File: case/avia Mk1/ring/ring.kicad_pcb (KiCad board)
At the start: 2 copper layers, 44 x 43.6 mm, 1 part

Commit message: corrected ring
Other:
- board text added: "avia ring v1.1"
- board text removed: "avia ring v1.0"
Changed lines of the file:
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@@
   (gr_line (start 162.476247 110.034954) (end 162.233575 109.716945) (layer "F.SilkS") (width 0.12))
   (gr_line (start 167.756337 103.786811) (end 167.401359 103.602393) (layer "F.SilkS") (width 0.12))
-  (gr_line (start 152.67 78.22) (end 153.48 78.32) (layer "F.SilkS") (width 0.1))
   (gr_line (start 157.675734 77.525941) (end 157.537261 77.901234) (layer "F.SilkS") (width 0.12))
   (gr_line (start 150.354831 113.833576) (end 150.370555 113.433861) (layer "F.SilkS") (width 0.12))
   (gr_line (start 145.720647 77.150237) (end 145.83725 77.53289) (layer "F.SilkS") (width 0.12))
   (gr_line (start 166.93 101.14) (end 167.02 101.18) (layer "F.SilkS") (width 0.12))
-  (gr_line (start 152.594209 79.031849) (end 152.67 78.22) (layer "F.SilkS") (width 0.1))
   (gr_line (start 132.492692 93.140089) (end 133.387785 93.234167) (layer "F.SilkS") (width 0.12))
   (gr_line (start 168.268998 102.726321) (end 167.446786 102.360249) (layer "F.SilkS") (width 0.12))
@@
     (effects (font (size 0.5 1.5) (thickness 0.125)))
   )
-  (gr_text "avia ring v1.0" (at 156.29 111.37) (layer "B.SilkS")
+  (gr_text "avia ring v1.1" (at 156.29 111.37) (layer "B.SilkS")
     (effects (font (size 0.6 1) (thickness 0.15)) (justify left mirror))
   )
@@
     (effects (font (size 0.7 1) (thickness 0.12)))
   )
-  (gr_text "KM" (at 154.06 78.17 -10.09) (layer "F.SilkS")
-    (effects (font (size 0.5 0.5) (thickness 0.08)))
-  )
   (gr_text "|" (at 135.542933 98.078105 100.81) (layer "F.SilkS")

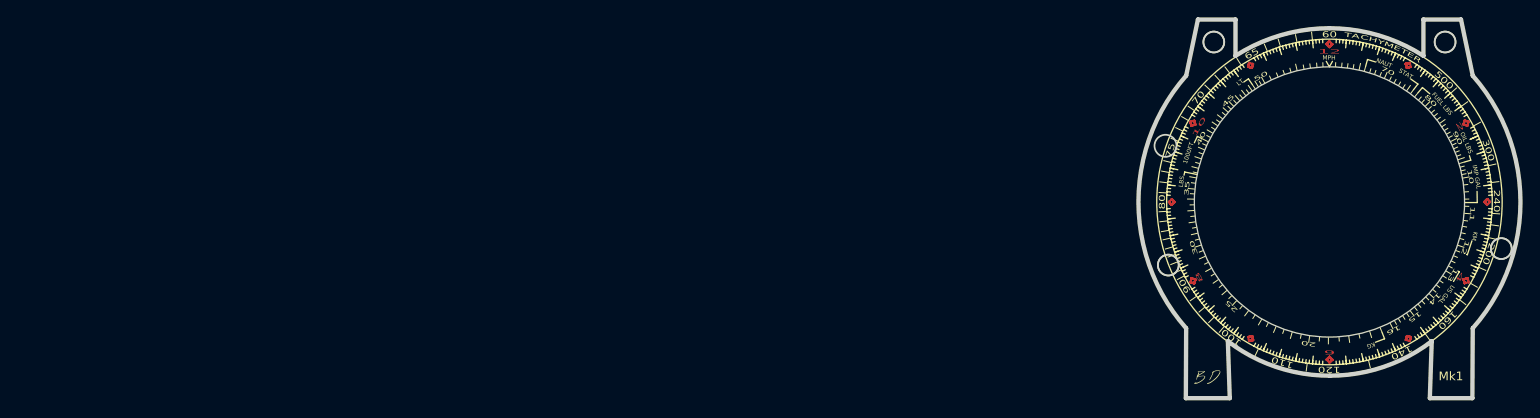
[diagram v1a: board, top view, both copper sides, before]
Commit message: added SR manual
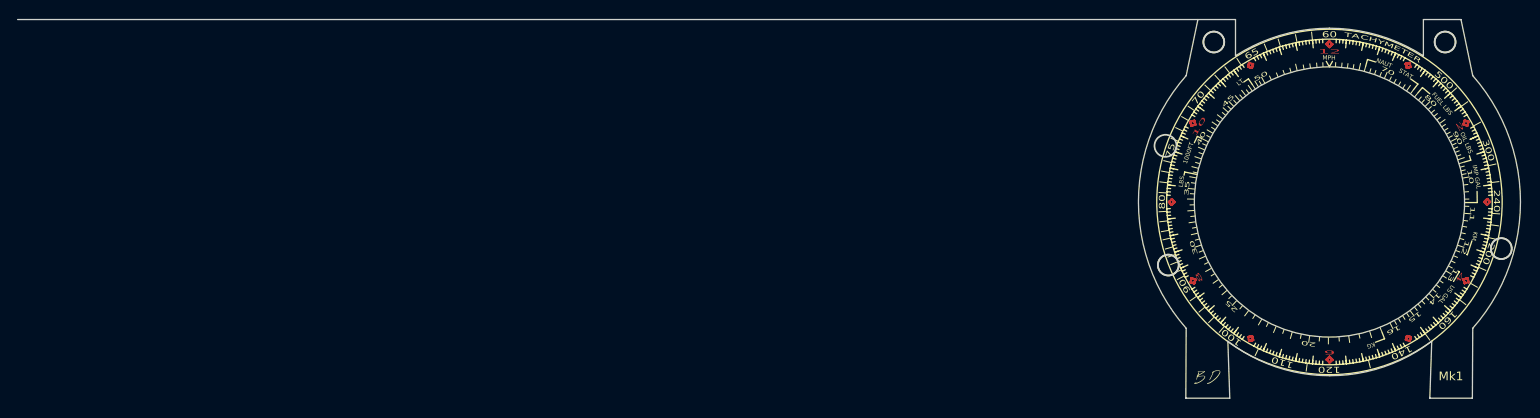
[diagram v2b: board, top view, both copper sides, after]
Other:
- board size 44 x 43.6 mm -> 173.1 x 43.6 mm
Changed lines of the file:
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@@
   (gr_line (start 137.64 108.6) (end 137.64 81.6) (layer "Cmts.User") (width 0.15))
   (gr_circle (center 164.46 76.68) (end 166.759609 76.68) (layer "Cmts.User") (width 0.15) (fill none))
+  (gr_circle (center 170.94 100.47) (end 173.239609 100.47) (layer "Cmts.User") (width 0.15) (fill none))
   (gr_line (start 167.04 79.2) (end 135.24 111) (layer "Cmts.User") (width 0.15))
   (gr_line (start 167.04 79.2) (end 167.04 116.52) (layer "Cmts.User") (width 0.15))
@@
   (gr_line (start 137.64 81.6) (end 137.64 79.2) (layer "Cmts.User") (width 0.15))
   (gr_line (start 137.64 81.6) (end 164.64 81.6) (layer "Cmts.User") (width 0.15))
-  (gr_arc (start 167.643267 80.553709) (mid 173.138918 95.100001) (end 167.643266 109.646293) (layer "Edge.Cuts") (width 0.5))
-  (gr_arc (start 151.18 115.11) (mid 144.981345 114.096892) (end 139.44 111.14) (layer "Edge.Cuts") (width 0.5))
-  (gr_line (start 162.92 111.14) (end 162.7 117.7) (layer "Edge.Cuts") (width 0.5))
-  (gr_arc (start 151.14 75.09) (mid 156.77909 75.901022) (end 161.961066 78.268344) (layer "Edge.Cuts") (width 0.5))
-  (gr_circle (center 151.14 95.1) (end 166.7 95.1) (layer "Edge.Cuts") (width 0.1) (fill none))
-  (gr_line (start 166.29 74.09) (end 167.643267 80.553709) (layer "Edge.Cuts") (width 0.5))
+  (gr_arc (start 167.643267 80.553709) (mid 173.139852 95.100001) (end 167.643266 109.646293) (layer "Edge.Cuts") (width 0.05))
+  (gr_arc (start 151.18 115.11) (mid 144.981385 114.096772) (end 139.44 111.14) (layer "Edge.Cuts") (width 0.05))
+  (gr_line (start 162.92 111.14) (end 162.7 117.7) (layer "Edge.Cuts") (width 0.05))
+  (gr_arc (start 151.14 75.09) (mid 156.778828 75.901912) (end 161.961066 78.268344) (layer "Edge.Cuts") (width 0.05))
+  (gr_circle (center 151.14 95.1) (end 166.7 95.1) (layer "Edge.Cuts") (width 0.05) (fill none))
+  (gr_line (start 166.29 74.09) (end 167.643267 80.553709) (layer "Edge.Cuts") (width 0.05))
   (gr_circle (center 132.58 102.37) (end 133.78 102.37) (layer "Edge.Cuts") (width 0.2) (fill none))
-  (gr_line (start 167.643266 109.646293) (end 167.6 117.7) (layer "Edge.Cuts") (width 0.5))
-  (gr_line (start 140.32 74.09) (end 140.32 78.27) (layer "Edge.Cuts") (width 0.5))
-  (gr_line (start 140.32 74.09) (end 135.99 74.09) (layer "Edge.Cuts") (width 0.5))
+  (gr_line (start 167.643266 109.646293) (end 167.6 117.7) (layer "Edge.Cuts") (width 0.05))
+  (gr_line (start 140.32 74.09) (end 140.32 78.27) (layer "Edge.Cuts") (width 0.05))
+  (gr_line (start 140.32 74.09) (end 0.05 74.09) (layer "Edge.Cuts") (width 0.05))
   (gr_circle (center 170.93 100.47) (end 172.13 100.47) (layer "Edge.Cuts") (width 0.2) (fill none))
-  (gr_line (start 161.96 74.09) (end 161.96 78.27) (layer "Edge.Cuts") (width 0.5))
-  (gr_line (start 139.66 117.7) (end 134.6 117.7) (layer "Edge.Cuts") (width 0.5))
-  (gr_arc (start 162.92 111.14) (mid 157.378655 114.096893) (end 151.18 115.11) (layer "Edge.Cuts") (width 0.5))
-  (gr_line (start 139.66 117.7) (end 139.44 111.14) (layer "Edge.Cuts") (width 0.5))
-  (gr_line (start 162.7 117.7) (end 167.6 117.7) (layer "Edge.Cuts") (width 0.5))
-  (gr_arc (start 140.318935 78.268344) (mid 145.500911 75.901022) (end 151.14 75.09) (layer "Edge.Cuts") (width 0.5))
-  (gr_line (start 134.636734 109.646293) (end 134.6 117.7) (layer "Edge.Cuts") (width 0.5))
-  (gr_line (start 135.99 74.09) (end 134.640001 80.550001) (layer "Edge.Cuts") (width 0.5))
+  (gr_line (start 161.96 74.09) (end 161.96 78.27) (layer "Edge.Cuts") (width 0.05))
+  (gr_line (start 139.66 117.7) (end 134.6 117.7) (layer "Edge.Cuts") (width 0.05))
+  (gr_arc (start 162.92 111.14) (mid 157.378615 114.096772) (end 151.18 115.11) (layer "Edge.Cuts") (width 0.05))
+  (gr_line (start 139.66 117.7) (end 139.44 111.14) (layer "Edge.Cuts") (width 0.05))
+  (gr_line (start 162.7 117.7) (end 167.6 117.7) (layer "Edge.Cuts") (width 0.05))
+  (gr_arc (start 140.318935 78.268344) (mid 145.501172 75.901912) (end 151.14 75.09) (layer "Edge.Cuts") (width 0.05))
+  (gr_line (start 134.636734 109.646293) (end 134.6 117.7) (layer "Edge.Cuts") (width 0.05))
+  (gr_line (start 135.99 74.09) (end 134.640001 80.550001) (layer "Edge.Cuts") (width 0.05))
   (gr_circle (center 137.82 76.68) (end 139.02 76.68) (layer "Edge.Cuts") (width 0.2) (fill none))
-  (gr_arc (start 134.636734 109.646293) (mid 129.141081 95.09753) (end 134.640001 80.550001) (layer "Edge.Cuts") (width 0.5))
+  (gr_arc (start 134.636734 109.646293) (mid 129.141081 95.09753) (end 134.640001 80.550001) (layer "Edge.Cuts") (width 0.05))
   (gr_circle (center 164.46 76.68) (end 165.66 76.68) (layer "Edge.Cuts") (width 0.2) (fill none))
   (gr_circle (center 132.259998 88.631545) (end 133.529998 88.631545) (layer "Edge.Cuts") (width 0.2) (fill none))
-  (gr_line (start 161.96 74.09) (end 166.29 74.09) (layer "Edge.Cuts") (width 0.5))
+  (gr_line (start 161.96 74.09) (end 166.29 74.09) (layer "Edge.Cuts") (width 0.05))
   (gr_circle (center 151.14 95.1) (end 157.89 106.791343) (layer "User.2") (width 0.2) (fill none))
   (gr_circle (center 151.14 95.1) (end 164.64 95.1) (layer "User.2") (width 0.2) (fill none))
